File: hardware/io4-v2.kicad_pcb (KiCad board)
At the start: 2 copper layers, 35 x 35 mm, 28 parts, among them J1 AKL_5_2, J2 AKL_5_2, J3 AKL_5_2, J4 AKL_5_2, J5 AKL_5_2, P1 CON-SENSOR2, P2 DEBUG, P3 BOOT, U1 XMC1100, U2 DRILL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

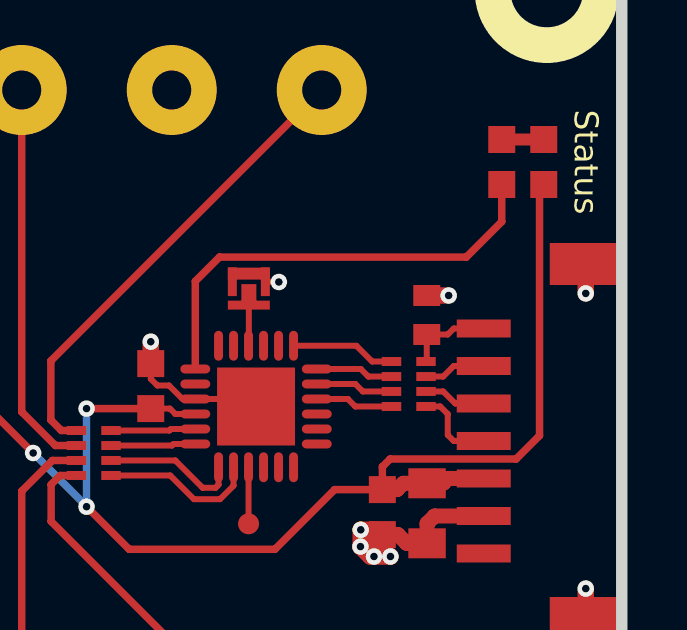
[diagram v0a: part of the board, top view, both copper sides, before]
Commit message: Change capacitor footprint(s) to C0402F
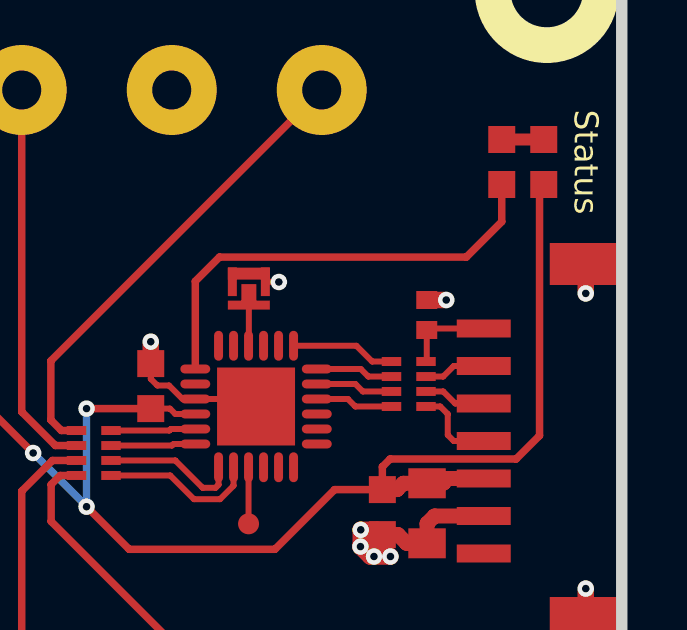
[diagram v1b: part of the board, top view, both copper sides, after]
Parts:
- C1: footprint C0402E -> kicad-libraries:C0402F
- C2: footprint C0805 -> kicad-libraries:C0805
- C3, C4: footprint C0603F -> kicad-libraries:C0603F
- D1: footprint D0603F -> kicad-libraries:D0603F
- J1, J2, J3, J4, J5: footprint AKL_5_2 -> kicad-libraries:AKL_5_2
- P1: footprint CON-SENSOR2 -> kicad-libraries:CON-SENSOR2
- P3: footprint SolderJumper -> kicad-libraries:SolderJumper
- R1: footprint R0603F -> kicad-libraries:R0603F
- RP1: value 100 -> 82; footprint 4X0402 -> kicad-libraries:4X0402
- RP2: footprint 4X0402 -> kicad-libraries:4X0402
- U2, U3, U4, U5: footprint DRILL_NP -> kicad-libraries:DRILL_NP
